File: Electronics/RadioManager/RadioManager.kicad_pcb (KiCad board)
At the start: 2 copper layers, 9 parts, among them J1 RJ45-MAG-LED, J2 RJ45-MAG-LED, J3 RJ45-MAG-LED, J4 RJ45-MAG-LED, J5 RJ45-MAG-LED, U1 KSZ8995FQI, U2 SC4503, U3 AOZ1280, U4 AOZ1280

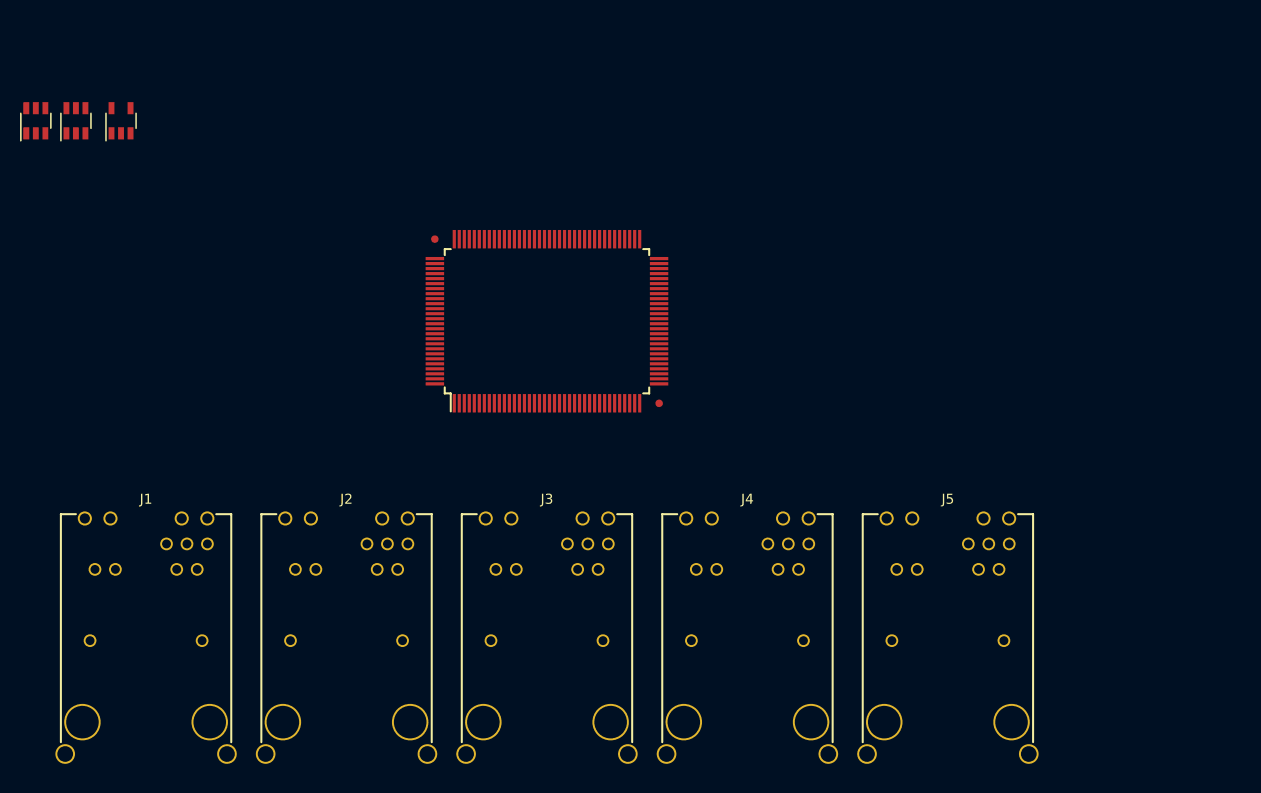
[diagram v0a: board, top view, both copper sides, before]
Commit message: Add missing decoupling cap
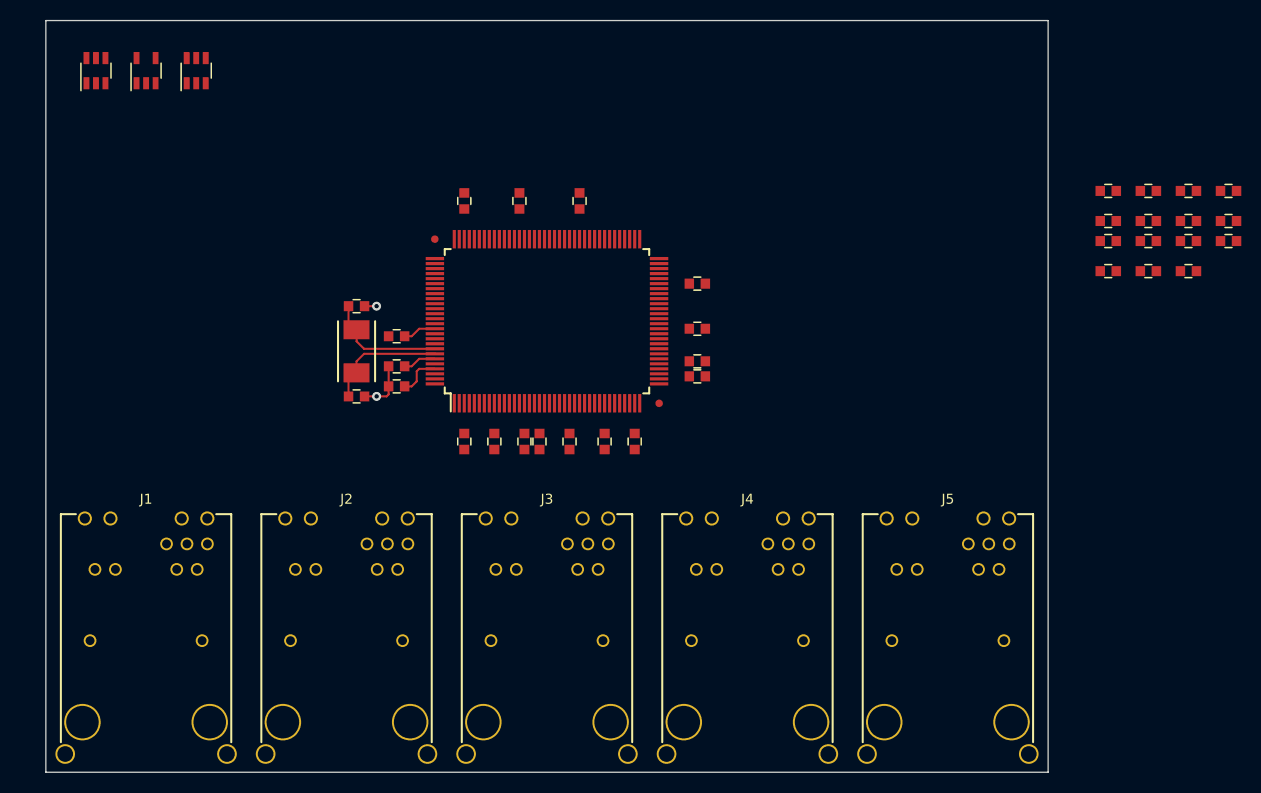
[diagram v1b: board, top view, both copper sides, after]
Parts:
- added C1: C, CAPC1608-N, F.Cu at (245.0, 114.5)
- added C10: C, CAPC1608-N, F.Cu at (245.0, 111.5)
- added C11: C, CAPC1608-N, F.Cu at (275.0, 115.5)
- added C12: C, CAPC1608-N, F.Cu at (254.8, 122.0)
- added C13: C, CAPC1608-N, F.Cu at (275.0, 114.0)
- added C14: C, CAPC1608-N, F.Cu at (259.2, 122.0)
- added C15: C, CAPC1608-N, F.Cu at (245.0, 116.5)
- added C16: C, CAPC1608-N, F.Cu at (262.2, 122.0)
- added C2: C, CAPC1608-N, F.Cu at (251.8, 122.0)
- added C22: 33pF, CAPC1608-N, F.Cu at (241.0, 108.5)
- added C23: 33pF, CAPC1608-N, F.Cu at (241.0, 117.5)
- added C3: C, CAPC1608-N, F.Cu at (275.0, 106.2)
- added C30: C, CAPC1608-N, F.Cu at (268.8, 122.0)
- added C4: C, CAPC1608-N, F.Cu at (275.0, 110.8)
- added C5: C, CAPC1608-N, F.Cu at (257.8, 122.0)
- added C6: C, CAPC1608-N, F.Cu at (263.2, 98.0)
- added C7: C, CAPC1608-N, F.Cu at (257.2, 98.0)
- added C8: C, CAPC1608-N, F.Cu at (265.8, 122.0)
- added C9: C, CAPC1608-N, F.Cu at (251.8, 98.0)
- added R1: R, RESC1608-N, F.Cu at (324.0, 105.0)
- added R10: R, RESC1608-N, F.Cu at (320.0, 105.0)
- added R11: R, RESC1608-N, F.Cu at (316.0, 102.0)
- added R12: R, RESC1608-N, F.Cu at (320.0, 100.0)
- added R13: R, RESC1608-N, F.Cu at (328.0, 97.0)
- added R14: R, RESC1608-N, F.Cu at (316.0, 105.0)
- added R15: R, RESC1608-N, F.Cu at (328.0, 102.0)
- added R2: R, RESC1608-N, F.Cu at (320.0, 102.0)
- added R3: R, RESC1608-N, F.Cu at (324.0, 102.0)
- added R4: 10k, RESC1608-N, F.Cu at (324.0, 97.0)
- added R5: 3.01k, RESC1608-N, F.Cu at (316.0, 97.0)
- added R6: 10k, RESC1608-N, F.Cu at (320.0, 97.0)
- added R7: 10k, RESC1608-N, F.Cu at (324.0, 100.0)
- added R8: 10k, RESC1608-N, F.Cu at (328.0, 100.0)
- added R9: 10k, RESC1608-N, F.Cu at (316.0, 100.0)
- added X1: 25MHz, XTAL-2SMD-60x35, F.Cu at (241.0, 113.0)
- moved U4 16.8 mm to (225.0, 85.0)
- moved U2 5.59 mm to (220.0, 85.0)
- moved U3 5.39 mm to (215.0, 85.0)
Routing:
- net /Switch/XO: track 0.00 -> 12.0 mm
- net /Switch/XI: track 0.00 -> 12.0 mm
- net +1.8V: track 0.00 -> 11.0 mm
- net GND: track 0.00 -> 6.48 mm, vias 0 -> 2
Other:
- board outline added: 100 x 75 mm

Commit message: Connect LEDs
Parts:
- added R16: R, RESC1608-N, F.Cu at (225.0, 127.5)
- added R17: R, RESC1608-N, F.Cu at (215.0, 127.5)
- added R18: R, RESC1608-N, F.Cu at (245.0, 127.5)
- added R19: R, RESC1608-N, F.Cu at (235.0, 127.5)
- added R20: R, RESC1608-N, F.Cu at (265.0, 127.5)
- added R21: R, RESC1608-N, F.Cu at (255.0, 127.5)
- added R22: R, RESC1608-N, F.Cu at (285.0, 127.5)
- added R23: R, RESC1608-N, F.Cu at (275.0, 127.5)
- added R24: R, RESC1608-N, F.Cu at (305.0, 127.5)
- added R25: R, RESC1608-N, F.Cu at (295.0, 127.5)
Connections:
- J1 pad 12: (no net) -> /Switch/SPD1
- J1 pad 13: (no net) -> N-0000047
- J1 pad 14: (no net) -> GND
- J1 pad 15: (no net) -> N-0000048
- J2 pad 12: (no net) -> /Switch/SPD2
- J2 pad 13: (no net) -> N-0000028
- J2 pad 14: (no net) -> GND
- J2 pad 15: (no net) -> N-0000029
- J3 pad 12: (no net) -> /Switch/SPD3
- J3 pad 13: (no net) -> N-0000041
- J3 pad 14: (no net) -> GND
- J3 pad 15: (no net) -> N-0000042
- J4 pad 12: (no net) -> /Switch/SPD4
- J4 pad 13: (no net) -> N-0000044
- J4 pad 14: (no net) -> GND
- J4 pad 15: (no net) -> N-0000043
- J5 pad 12: (no net) -> /Switch/SPD5
- J5 pad 13: (no net) -> N-0000046
- J5 pad 14: (no net) -> GND
- J5 pad 15: (no net) -> N-0000045
- U1 pad 101: (no net) -> /Switch/ACT2
- U1 pad 103: (no net) -> /Switch/SPD2
- U1 pad 104: (no net) -> /Switch/ACT1
- U1 pad 106: (no net) -> /Switch/SPD1
- U1 pad 90: (no net) -> /Switch/ACT5
- U1 pad 92: (no net) -> /Switch/SPD5
- U1 pad 93: (no net) -> /Switch/ACT4
- U1 pad 95: (no net) -> /Switch/SPD4
- U1 pad 96: (no net) -> /Switch/ACT3
- U1 pad 98: (no net) -> /Switch/SPD3

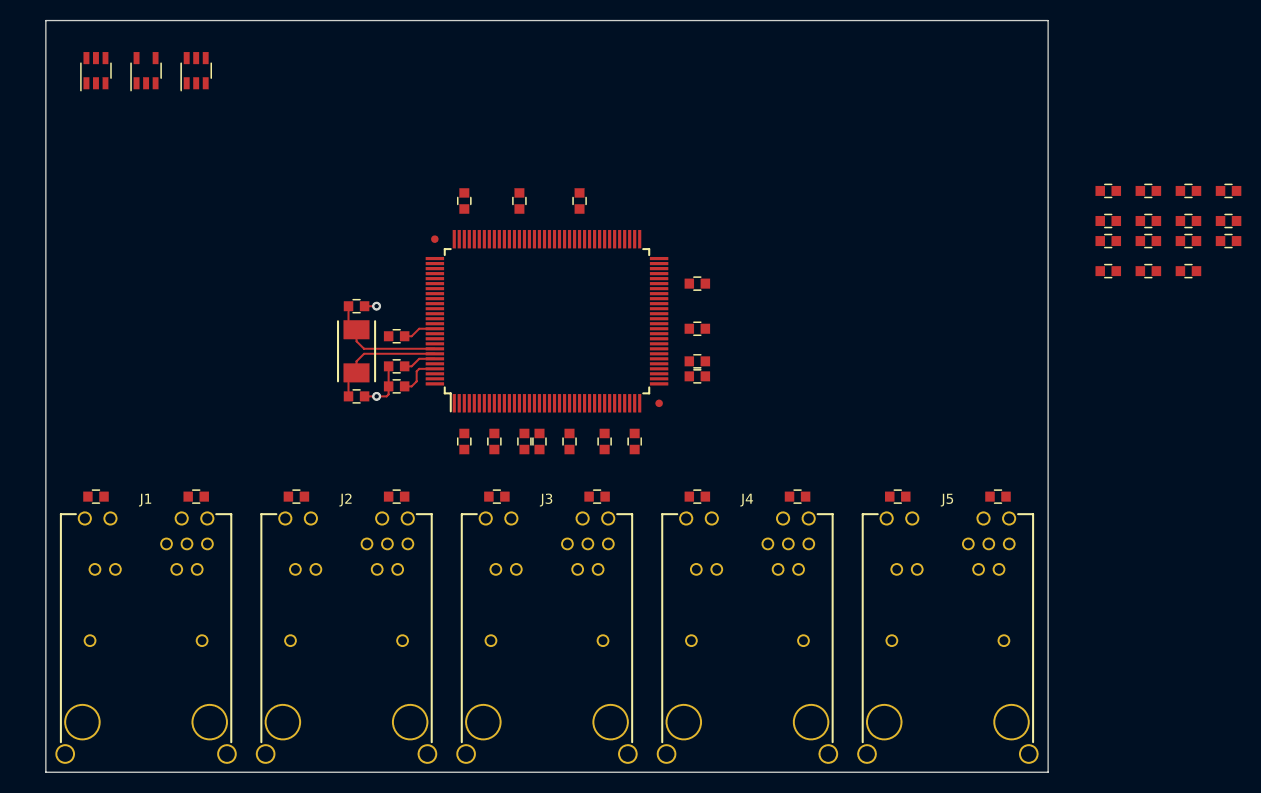
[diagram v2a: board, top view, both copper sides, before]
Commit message: Change board form factor
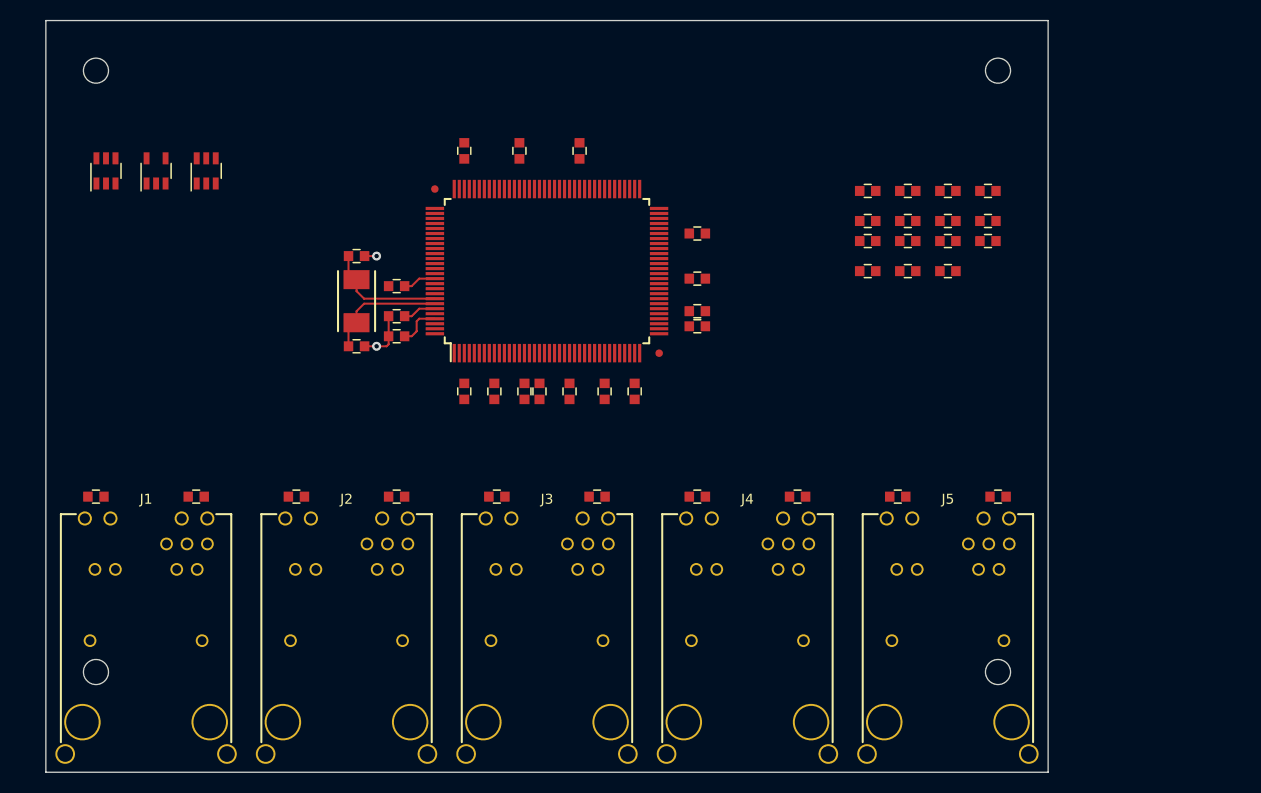
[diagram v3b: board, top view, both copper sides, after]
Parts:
- added MECH-JIG250: VAL**, MECH-JIG250, F.Cu at (305.0, 145.0)
- added MECH-JIG250: VAL**, MECH-JIG250, F.Cu at (215.0, 145.0)
- added MECH-JIG250: VAL**, MECH-JIG250, F.Cu at (215.0, 85.0)
- added MECH-JIG250: VAL**, MECH-JIG250, F.Cu at (305.0, 85.0)
- moved R1 24.0 mm to (300.0, 105.0)
- moved R10 24.0 mm to (296.0, 105.0)
- moved R11 24.0 mm to (292.0, 102.0)
- moved R12 24.0 mm to (296.0, 100.0)
- moved R13 24.0 mm to (304.0, 97.0)
- moved R14 24.0 mm to (292.0, 105.0)
- moved R15 24.0 mm to (304.0, 102.0)
- moved R2 24.0 mm to (296.0, 102.0)
- moved R3 24.0 mm to (300.0, 102.0)
- moved R4 24.0 mm to (300.0, 97.0)
- moved R5 24.0 mm to (292.0, 97.0)
- moved R6 24.0 mm to (296.0, 97.0)
- moved R7 24.0 mm to (300.0, 100.0)
- moved R8 24.0 mm to (304.0, 100.0)
- moved R9 24.0 mm to (292.0, 100.0)
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
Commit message: Swap tx/rx pairs for better routing
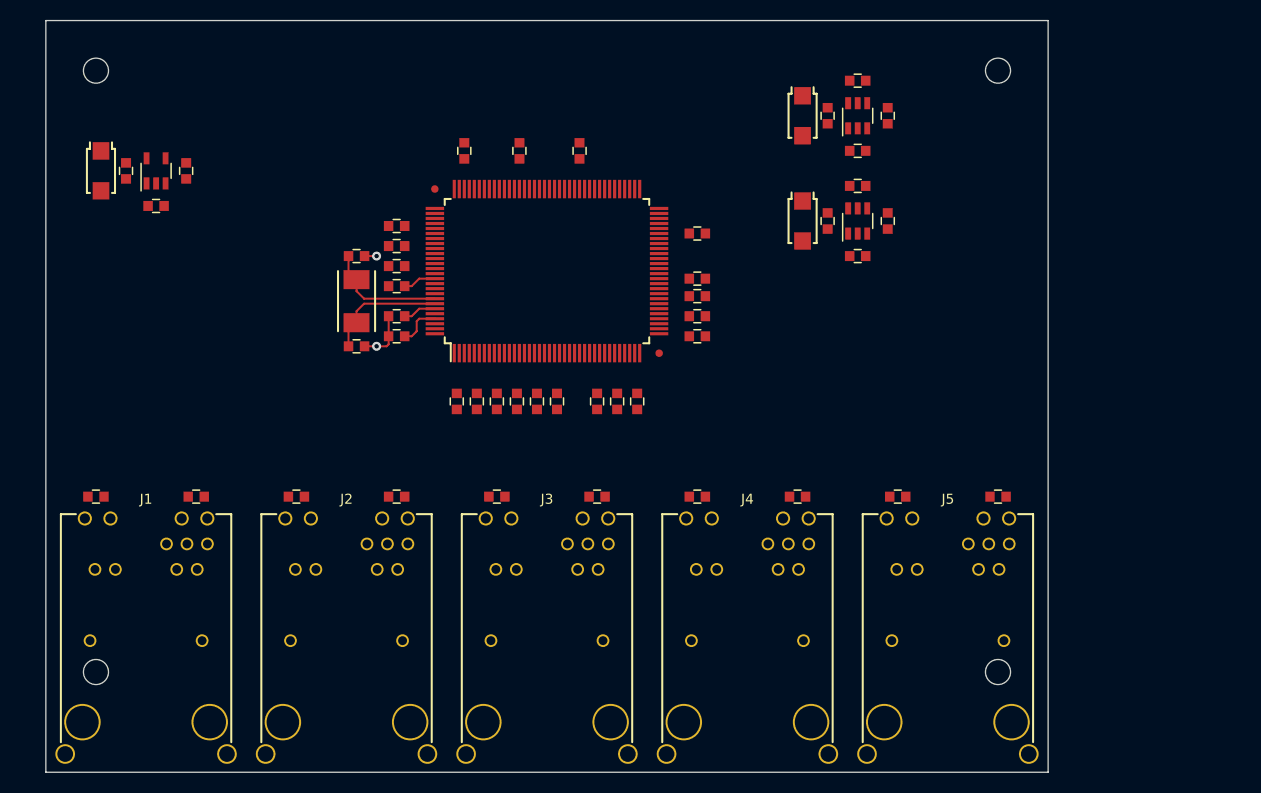
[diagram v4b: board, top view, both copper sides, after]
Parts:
- added C26: 10000pF, CAPC1608-N, F.Cu at (288.0, 89.5)
- added C27: 10000pF, CAPC1608-N, F.Cu at (288.0, 100.0)
- added D1: CDBA140, SODFL5126-N, F.Cu at (215.5, 95.0)
- added D3: CDBA140, SODFL5126-N, F.Cu at (285.5, 89.5)
- added D4: CDBA140, SODFL5126-N, F.Cu at (285.5, 100.0)
- R12: value R -> 49.9k
- R13: value R -> 15.8k
- R14: value R -> 80.6k
- R15: value R -> 64.2k
- moved R3 79.1 mm to (221.0, 98.5)
- moved R2 78.3 mm to (218.0, 95.0), turned to 90 degrees
- moved R1 76.7 mm to (224.0, 95.0), turned to 90 degrees
- moved U3 75.2 mm to (291.0, 89.5)
- moved U4 65.2 mm to (291.0, 100.0)
- moved R8 59.0 mm to (245.0, 100.5)
- moved R7 55.1 mm to (245.0, 102.5)
- moved R6 49.7 mm to (251.0, 118.0), turned to 90 degrees
- moved R9 47.2 mm to (245.0, 104.5), turned to 180 degrees
- moved R5 39.1 mm to (259.0, 118.0), turned to 90 degrees
- moved R4 27.1 mm to (275.0, 107.5)
- moved R10 19.6 mm to (291.0, 86.0)
- moved R13 12.5 mm to (294.0, 89.5), turned to 270 degrees
- moved R15 10.2 mm to (294.0, 100.0), turned to 270 degrees
- moved R12 8.60 mm to (291.0, 93.0), turned to 180 degrees
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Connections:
- U1 pad 10: /Switch/RXP2 -> /Switch/TXP2
- U1 pad 11: /Switch/RXM2 -> /Switch/TXM2
- U1 pad 13: /Switch/TXP2 -> /Switch/RXP2
- U1 pad 14: /Switch/TXM2 -> /Switch/RXM2
- U1 pad 19: /Switch/RXP3 -> /Switch/TXP3
- U1 pad 20: /Switch/RXM3 -> /Switch/TXM3
- U1 pad 22: /Switch/TXP3 -> /Switch/RXP3
- U1 pad 23: /Switch/TXM3 -> /Switch/RXM3
- U1 pad 25: /Switch/RXP4 -> /Switch/TXP4
- U1 pad 26: /Switch/RXM4 -> /Switch/TXM4
- U1 pad 28: /Switch/TXP4 -> /Switch/RXP4
- U1 pad 29: /Switch/TXM4 -> /Switch/RXM4
- U1 pad 32: /Switch/RXP5 -> /Switch/TXP5
- U1 pad 33: /Switch/RXM5 -> /Switch/TXM5
- U1 pad 35: /Switch/TXP5 -> /Switch/RXP5
- U1 pad 36: /Switch/TXM5 -> /Switch/RXM5
- U1 pad 4: /Switch/RXP1 -> /Switch/TXP1
- U1 pad 5: /Switch/RXM1 -> /Switch/TXM1
- U1 pad 7: /Switch/TXP1 -> /Switch/RXP1
- U1 pad 8: /Switch/TXM1 -> /Switch/RXM1
